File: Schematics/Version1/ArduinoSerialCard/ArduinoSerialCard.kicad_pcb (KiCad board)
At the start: 2 copper layers, 50.8 x 27.9 mm, 2 parts, among them J1 Conn

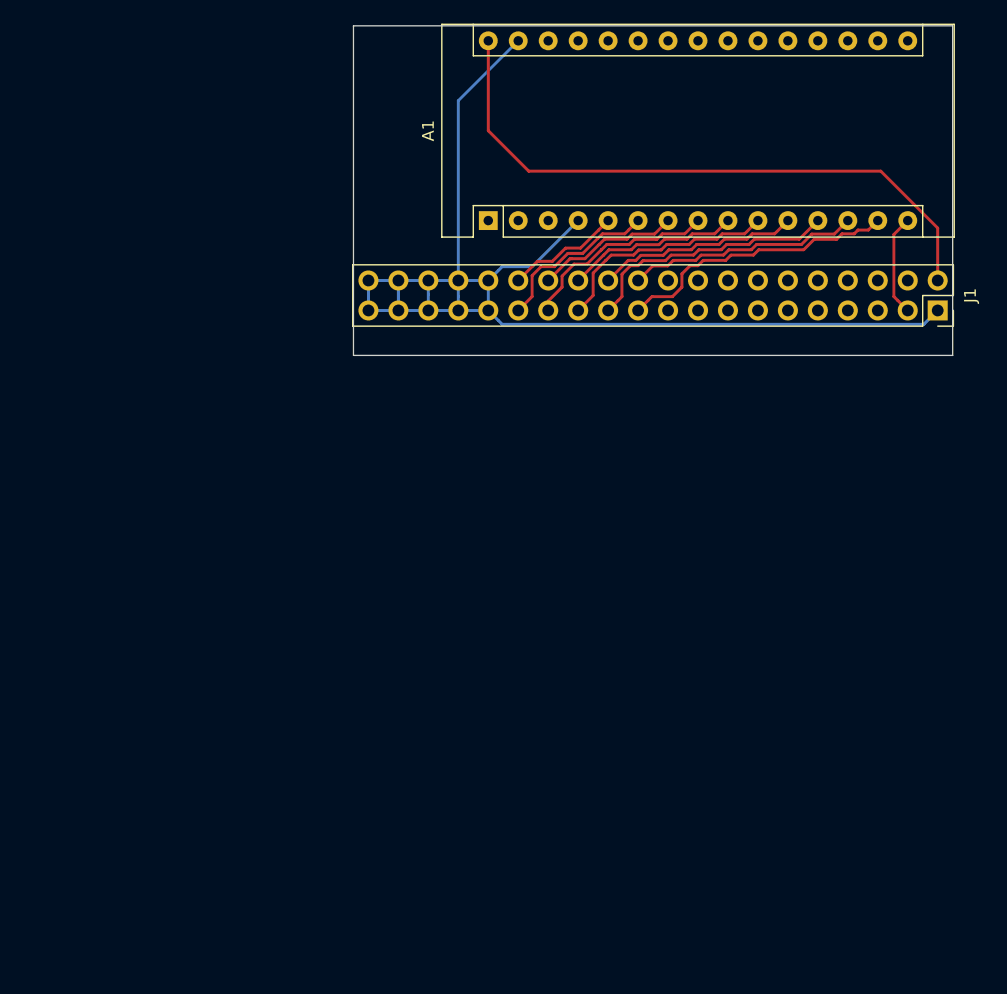
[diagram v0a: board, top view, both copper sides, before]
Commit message: Update the Arduino serial card to use revised schematic.
This is the design for which I've written the latest Arduino sketch, and
the prototype works wonderfully. Basically, it includes three memory mapped
registers which acts as intermediaries between the Arduino and the CPU.
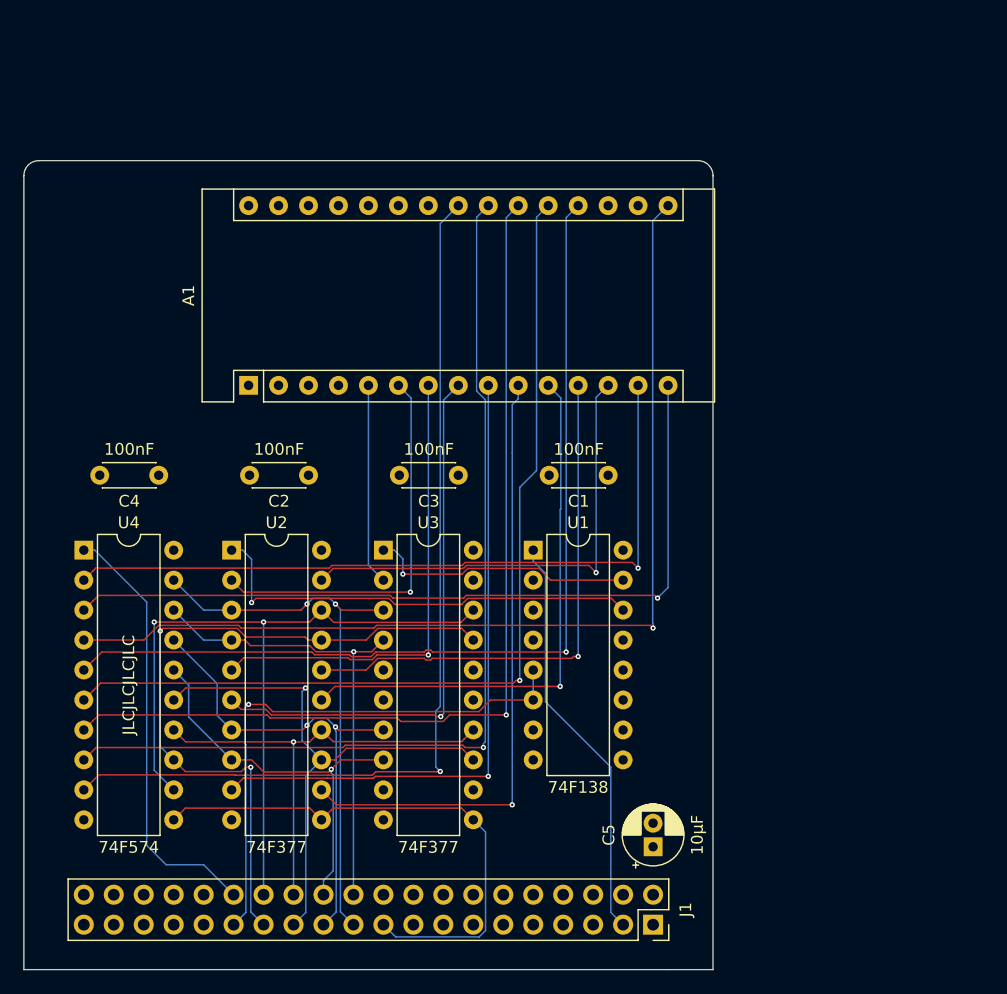
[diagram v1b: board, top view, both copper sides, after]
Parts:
- added C1: 100nF, Capacitor_THT:C_Disc_D4.3mm_W1.9mm_P5.00mm, F.Cu at (157.5, 95.2)
- added C2: 100nF, Capacitor_THT:C_Disc_D4.3mm_W1.9mm_P5.00mm, F.Cu at (132.1, 95.2)
- added C3: 100nF, Capacitor_THT:C_Disc_D4.3mm_W1.9mm_P5.00mm, F.Cu at (144.8, 95.2)
- added C4: 100nF, Capacitor_THT:C_Disc_D4.3mm_W1.9mm_P5.00mm, F.Cu at (119.4, 95.2)
- added C5: 10µF, Capacitor_THT:CP_Radial_D5.0mm_P2.00mm, F.Cu at (161.3, 126.7)
- added U1: 74F138, Package_DIP:DIP-16_W7.62mm, F.Cu at (151.1, 101.6)
- added U2: 74F377, Package_DIP:DIP-20_W7.62mm, F.Cu at (125.6, 101.6)
- added U3: 74F377, Package_DIP:DIP-20_W7.62mm, F.Cu at (138.4, 101.6)
- added U4: 74F574, Package_DIP:DIP-20_W7.62mm, F.Cu at (113.0, 101.6)
- moved J1 57.4 mm to (161.3, 133.3)
- moved A1 24.7 mm to (127.0, 87.6)
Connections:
- A1 pad 10: /DataBus4 -> Net-(A1-Pad10)
- A1 pad 11: /DataBus3 -> Net-(A1-Pad11)
- A1 pad 12: /DataBus2 -> Net-(A1-Pad12)
- A1 pad 13: /DataBus1 -> Net-(A1-Pad13)
- A1 pad 14: /DataBus0 -> Net-(A1-Pad14)
- A1 pad 15: /AddressBus0 -> Net-(A1-Pad15)
- A1 pad 16: (no net) -> Net-(A1-Pad16)
- A1 pad 19: (no net) -> Net-(A1-Pad19)
- A1 pad 20: (no net) -> Net-(A1-Pad20)
- A1 pad 21: (no net) -> Net-(A1-Pad21)
- A1 pad 22: (no net) -> Net-(A1-Pad22)
- A1 pad 23: (no net) -> Net-(A1-Pad23)
- A1 pad 30: VCC -> (no net)
- A1 pad 5: /~PO -> Net-(A1-Pad5)
- A1 pad 6: /~PI -> Net-(A1-Pad6)
- A1 pad 7: /DataBus7 -> Net-(A1-Pad7)
- A1 pad 8: /DataBus6 -> Net-(A1-Pad8)
- A1 pad 9: /DataBus5 -> Net-(A1-Pad9)
- J1 pad 19: (no net) -> /RegisterClock
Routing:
- net GND: track 104.2 -> 0.00 mm
- net Net-(A1-Pad16): track 0.00 -> 85.4 mm, vias 0 -> 1
- net Net-(A1-Pad22): track 0.00 -> 81.2 mm, vias 0 -> 1
- net Net-(A1-Pad21): track 0.00 -> 80.4 mm, vias 0 -> 1
- net Net-(A1-Pad19): track 0.00 -> 80.2 mm, vias 0 -> 1
- net Net-(A1-Pad23): track 0.00 -> 79.8 mm, vias 0 -> 1
- net Net-(A1-Pad20): track 0.00 -> 78.9 mm, vias 0 -> 1
- net Net-(A1-Pad15): track 0.00 -> 67.8 mm, vias 0 -> 1
- net Net-(A1-Pad14): track 0.00 -> 63.3 mm, vias 0 -> 1
- net Net-(A1-Pad9): track 0.00 -> 55.4 mm, vias 0 -> 1
- net /DataBus7: track 12.3 -> 66.4 mm, vias 0 -> 2
- net VCC: track 53.6 -> 0.00 mm
- net Net-(A1-Pad10): track 0.00 -> 52.5 mm, vias 0 -> 1
- net Net-(A1-Pad8): track 0.00 -> 47.0 mm, vias 0 -> 1
- net Net-(A1-Pad11): track 0.00 -> 46.7 mm, vias 0 -> 1
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- added copper zone on GND.Cu, net GND
- added copper zone on VCC.Cu, net VCC
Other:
- board size 50.8 x 27.9 mm -> 58.4 x 68.6 mm
- copper layers 2 -> 4
- net class Default: clearance 0.2 -> 0.127; trace_width 0.25 -> 0.127; via_dia 0.8 -> 0.45; via_drill 0.4 -> 0.2
- rule trace_clearance: 0.2 -> 0.127
- rule trace_min: 0.2 -> 0.0889
- rule via_min_drill: 0.3 -> 0.2
- rule via_min_size: 0.4 -> 0.45
- board text added: "JLCJLCJLCJLC"

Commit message: Fix the Arduino Serial Card PCB.
The Arduino serial card PCB had the enable pins wired incorrectly.
Fix this for revision 3.
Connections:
- U1 pad 4: VCC -> /~PI
- U1 pad 6: /~PI -> VCC
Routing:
- net /~PI: track 46.6 -> 49.1 mm, vias 1 -> 2
- added copper zone on In1.Cu, net GND
- added copper zone on In2.Cu, net VCC
- removed copper zone on GND.Cu, net GND
- removed copper zone on VCC.Cu, net VCC
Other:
- board text added: "Arduino Serial Interface © 2019 Andrew Fox, Rev 3"
- board text removed: "Arduino Serial Interface © 2019 Andrew Fox, Rev 2"
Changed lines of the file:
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@@
     (thickness 1.6)
     (drawings 9)
-    (tracks 360)
+    (tracks 366)
     (zones 0)
     (modules 11)
@@
   (layers
     (0 F.Cu signal)
-    (1 GND.Cu power hide)
-    (2 VCC.Cu power hide)
+    (1 In1.Cu power hide)
+    (2 In2.Cu power hide)
     (31 B.Cu signal)
     (32 B.Adhes user)
@@
       (net 33 "Net-(U1-Pad14)"))
     (pad 6 thru_hole oval (at 0 12.7) (size 1.6 1.6) (drill 0.8) (layers *.Cu *.Mask)
-      (net 13 /~PI))
+      (net 1 VCC))
     (pad 13 thru_hole oval (at 7.62 7.62) (size 1.6 1.6) (drill 0.8) (layers *.Cu *.Mask))
     (pad 5 thru_hole oval (at 0 10.16) (size 1.6 1.6) (drill 0.8) (layers *.Cu *.Mask)
@@
     (pad 12 thru_hole oval (at 7.62 10.16) (size 1.6 1.6) (drill 0.8) (layers *.Cu *.Mask))
     (pad 4 thru_hole oval (at 0 7.62) (size 1.6 1.6) (drill 0.8) (layers *.Cu *.Mask)
-      (net 1 VCC))
+      (net 13 /~PI))
     (pad 11 thru_hole oval (at 7.62 12.7) (size 1.6 1.6) (drill 0.8) (layers *.Cu *.Mask))
     (pad 3 thru_hole oval (at 0 5.08) (size 1.6 1.6) (drill 0.8) (layers *.Cu *.Mask)
@@
   (gr_line (start 166.37 137.16) (end 166.37 69.85) (layer Edge.Cuts) (width 0.05))
   (gr_line (start 162.56 137.16) (end 166.37 137.16) (layer Edge.Cuts) (width 0.05))
-  (gr_text "Arduino Serial Interface\n© 2019 Andrew Fox, Rev 2" (at 137.16 80.01) (layer B.SilkS)
+  (gr_text "Arduino Serial Interface\n© 2019 Andrew Fox, Rev 3" (at 137.16 80.01) (layer B.SilkS)
     (effects (font (size 1.5 1.5) (thickness 0.3)) (justify mirror))
   )
   (gr_line (start 107.95 137.16) (end 162.56 137.16) (layer Edge.Cuts) (width 0.05))
-  (segment (start 148.463 99.568) (end 148.463 96.774) (width 0.127) (layer GND.Cu) (net 0))
+  (segment (start 148.463 99.568) (end 148.463 96.774) (width 0.127) (layer In1.Cu) (net 0))
   (segment (start 151.13 101.6) (end 151.13 102.527) (width 0.127) (layer B.Cu) (net 3))
   (segment (start 151.13 102.527) (end 152.170501 103.567501) (width 0.127) (layer B.Cu) (net 3))
@@
   (segment (start 118.364 126.619) (end 120.015 128.27) (width 0.127) (layer B.Cu) (net 12))
   (segment (start 123.19 128.27) (end 120.015 128.27) (width 0.127) (layer B.Cu) (net 12))
-  (segment (start 151.13 111.76) (end 151.13 114.3) (width 0.127) (layer B.Cu) (net 13))
-  (segment (start 146.525441 115.290501) (end 129.057499 115.290501) (width 0.127) (layer F.Cu) (net 13))
-  (segment (start 147.515942 114.3) (end 146.525441 115.290501) (width 0.127) (layer F.Cu) (net 13))
-  (segment (start 151.13 114.3) (end 147.515942 114.3) (width 0.127) (layer F.Cu) (net 13))
-  (via (at 127 114.681) (size 0.45) (drill 0.2) (layers F.Cu B.Cu) (net 13))
-  (segment (start 128.447998 114.681) (end 127 114.681) (width 0.127) (layer F.Cu) (net 13))
-  (segment (start 129.057499 115.290501) (end 128.447998 114.681) (width 0.127) (layer F.Cu) (net 13))
-  (segment (start 127 114.681) (end 126.711499 114.969501) (width 0.127) (layer B.Cu) (net 13))
+  (segment (start 126.770501 132.309499) (end 126.770501 118.076503) (width 0.127) (layer B.Cu) (net 13))
+  (segment (start 126.711499 114.969501) (end 126.711499 118.017501) (width 0.127) (layer B.Cu) (net 13))
+  (segment (start 125.73 133.35) (end 126.770501 132.309499) (width 0.127) (layer B.Cu) (net 13))
   (segment (start 126.770501 118.076503) (end 126.711499 118.017501) (width 0.127) (layer B.Cu) (net 13))
-  (segment (start 125.73 133.35) (end 126.770501 132.309499) (width 0.127) (layer B.Cu) (net 13))
-  (segment (start 126.711499 114.969501) (end 126.711499 118.017501) (width 0.127) (layer B.Cu) (net 13))
-  (segment (start 126.770501 132.309499) (end 126.770501 118.076503) (width 0.127) (layer B.Cu) (net 13))
+  (via (at 126.746 114.684499) (size 0.45) (drill 0.2) (layers F.Cu B.Cu) (net 13))
+  (segment (start 126.711499 114.719) (end 126.746 114.684499) (width 0.127) (layer B.Cu) (net 13))
+  (segment (start 126.711499 114.969501) (end 126.711499 114.719) (width 0.127) (layer B.Cu) (net 13))
+  (via (at 149.987 115.189) (size 0.45) (drill 0.2) (layers F.Cu B.Cu) (net 13))
+  (segment (start 148.508557 115.290501) (end 148.644559 115.154499) (width 0.127) (layer F.Cu) (net 13))
+  (segment (start 148.644559 115.154499) (end 149.952499 115.154499) (width 0.127) (layer F.Cu) (net 13))
+  (segment (start 132.704559 115.290501) (end 148.508557 115.290501) (width 0.127) (layer F.Cu) (net 13))
+  (segment (start 132.098557 114.684499) (end 132.704559 115.290501) (width 0.127) (layer F.Cu) (net 13))
+  (segment (start 149.952499 115.154499) (end 149.987 115.189) (width 0.127) (layer F.Cu) (net 13))
+  (segment (start 126.746 114.684499) (end 132.098557 114.684499) (width 0.127) (layer F.Cu) (net 13))
+  (segment (start 149.987 113.263942) (end 151.13 112.120942) (width 0.127) (layer B.Cu) (net 13))
+  (segment (start 151.13 112.120942) (end 151.13 111.76) (width 0.127) (layer B.Cu) (net 13))
+  (segment (start 149.987 115.189) (end 149.987 113.263942) (width 0.127) (layer B.Cu) (net 13))
+  (segment (start 151.13 111.76) (end 151.13 109.22) (width 0.127) (layer B.Cu) (net 13))
   (segment (start 161.255498 107.788498) (end 161.255498 73.694502) (width 0.127) (layer B.Cu) (net 14))
   (segment (start 161.255498 73.694502) (end 162.56 72.39) (width 0.127) (layer B.Cu) (net 14))
@@
   (segment (start 127.254 102.367) (end 126.487 101.6) (width 0.127) (layer B.Cu) (net 33))
   (segment (start 127.254 106.045) (end 127.254 102.367) (width 0.127) (layer B.Cu) (net 33))
-  (zone (net 2) (net_name GND) (layer GND.Cu) (hatch edge 0.508)
+  (zone (net 2) (net_name GND) (layer In1.Cu) (hatch edge 0.508)
     (connect_pads (clearance 0.254))
     (min_thickness 0.254)
@@
     )
   )
-  (zone (net 1) (net_name VCC) (layer VCC.Cu) (hatch edge 0.508)
+  (zone (net 1) (net_name VCC) (layer In2.Cu) (hatch edge 0.508)
     (connect_pads (clearance 0.254))
     (min_thickness 0.254)
